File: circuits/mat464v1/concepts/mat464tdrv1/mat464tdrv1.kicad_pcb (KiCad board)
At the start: 2 copper layers, 107.2 x 67.3 mm, 41 parts, among them J1 Input 1, J10 GND VDC, J11 -VDC, J2 Input 2, J3 Input GND, J4 Zero crossing det, J5 Output 1, J6 Output 2, J7 Output GND, J8 Conn_WallSocket, J9 +VDC, Q1 BC547, Q2 BC547, U1 TL084

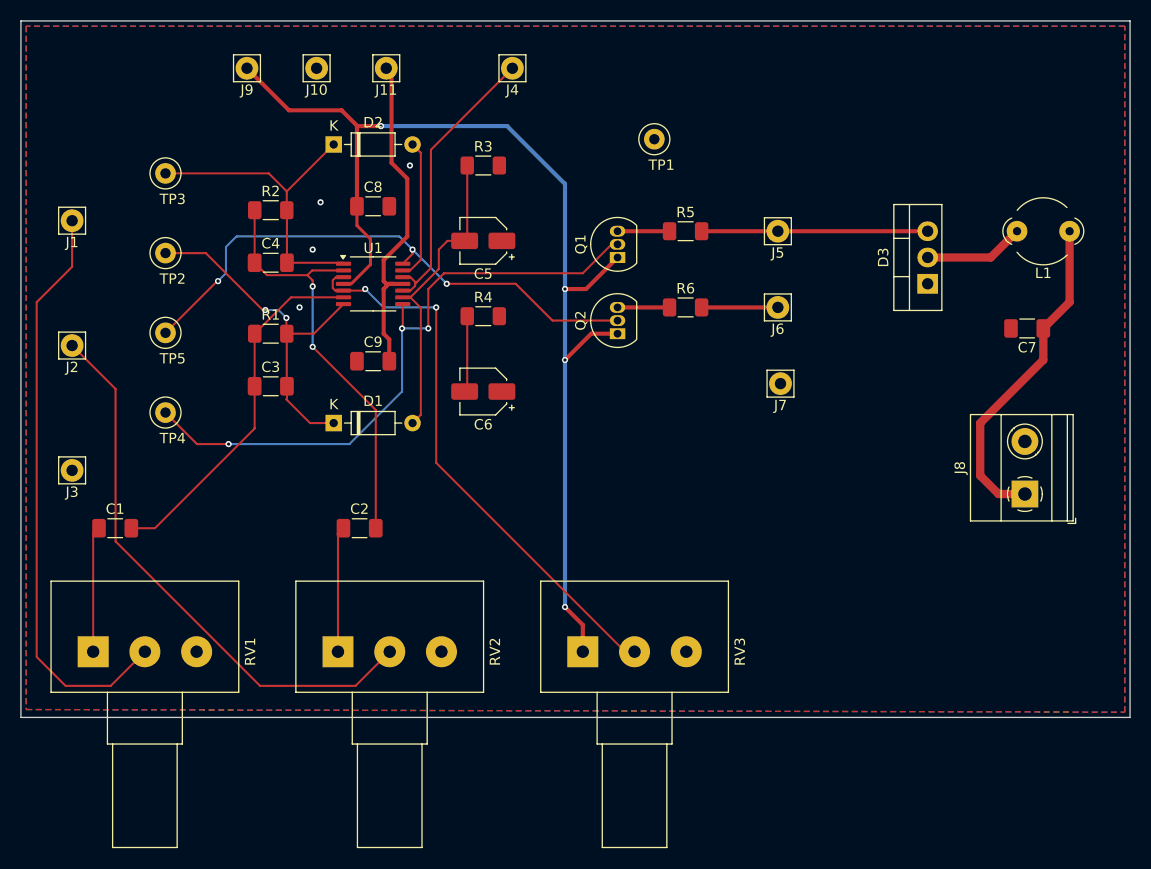
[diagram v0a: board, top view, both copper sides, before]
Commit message: Update the modern AT464 concept PCBs
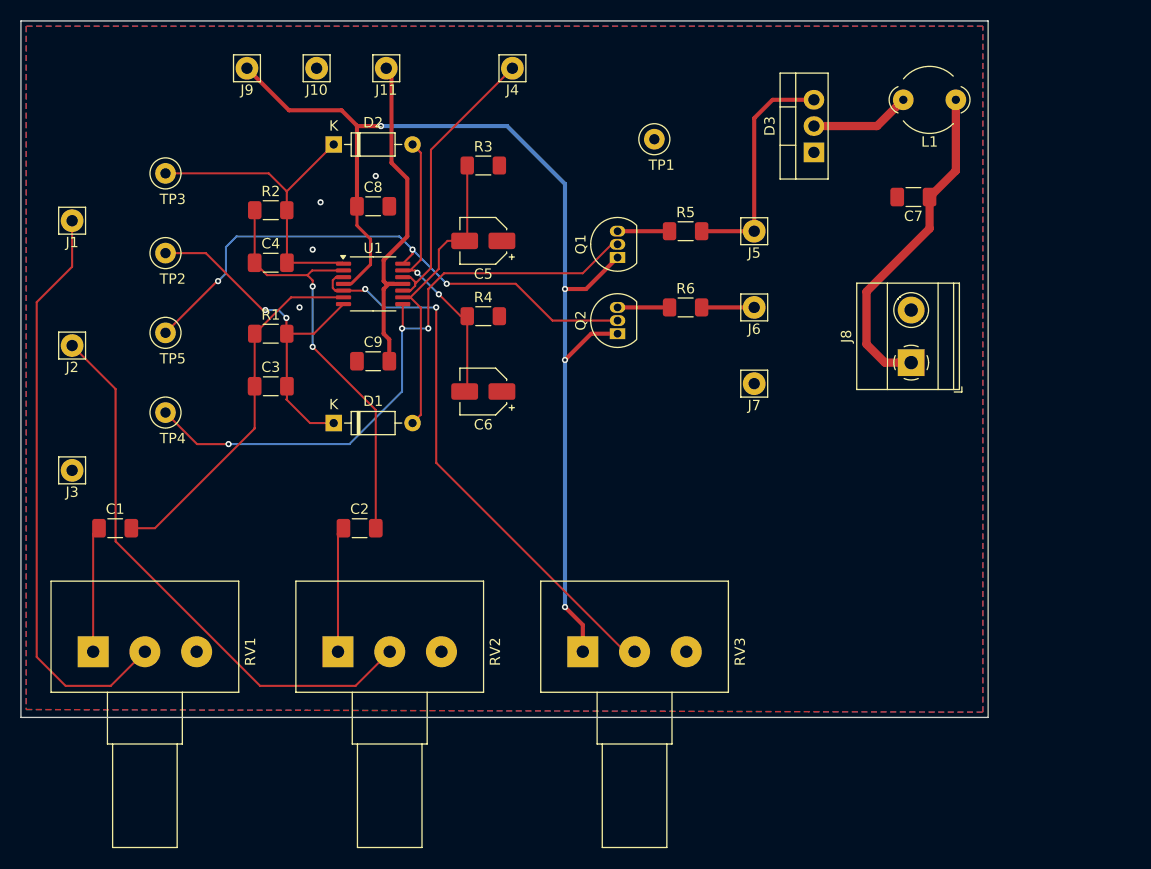
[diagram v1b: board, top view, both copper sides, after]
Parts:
- moved D3 16.8 mm to (134.3, 62.2)
- moved C7 16.8 mm to (143.9, 66.5)
- moved J8 16.8 mm to (143.7, 82.5)
- moved L1 16.8 mm to (148.0, 57.1)
- moved J7 2.54 mm to (128.5, 84.6)
- moved J5 2.29 mm to (128.5, 69.8)
- moved J6 2.29 mm to (128.5, 77.2)
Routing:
- net Net-(D2-A): track 21.0 -> 29.1 mm, vias 0 -> 2
- net Net-(J6-Pin_1): track 7.37 -> 5.08 mm
- net Net-(D3-G): track 21.8 -> 22.5 mm
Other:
- board size 107.2 x 67.3 mm -> 93.5 x 67.3 mm
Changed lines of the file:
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@@
 	(footprint "Capacitor_SMD:C_1206_3216Metric_Pad1.33x1.80mm_HandSolder"
 		(layer "F.Cu")
-		(at 154.9015 79.248 180)
+		(at 143.9085 66.548 180)
 		(descr "Capacitor SMD 1206 (3216 Metric), square (rectangular) end terminal, IPC_7351 nominal with elongated pad for handsoldering. (Body size source: IPC-SM-782 page 76, https://www.pcb-3d.com/wordpress/wp-content/uploads/ipc-sm-782a_amendment_1_and_2.pdf), generated with kicad-footprint-generator")
 		(tags "capacitor handsolder")
@@
 	(footprint "Connector_Pin:Pin_D1.1mm_L8.5mm_W2.5mm_FlatFork"
 		(layer "F.Cu")
-		(at 130.81 69.85)
+		(at 128.524 69.85)
 		(descr "solder Pin_ with flat fork, hole diameter 1.1mm, length 8.5mm, width 2.5mm")
 		(tags "solder Pin_ with flat fork")
@@
 	(footprint "Connector_Pin:Pin_D1.1mm_L8.5mm_W2.5mm_FlatFork"
 		(layer "F.Cu")
-		(at 130.81 77.216)
+		(at 128.524 77.216)
 		(descr "solder Pin_ with flat fork, hole diameter 1.1mm, length 8.5mm, width 2.5mm")
 		(tags "solder Pin_ with flat fork")
@@
 	(footprint "Package_TO_SOT_THT:TO-220-3_Vertical"
 		(layer "F.Cu")
-		(at 145.288 74.93 90)
+		(at 134.295 62.23 90)
 		(descr "TO-220-3, Vertical, RM 2.54mm, see https://www.vishay.com/docs/66542/to-220-1.pdf")
 		(tags "TO-220-3 Vertical RM 2.54mm")
@@
 	(footprint "TerminalBlock_Phoenix:TerminalBlock_Phoenix_MKDS-1,5-2-5.08_1x02_P5.08mm_Horizontal"
 		(layer "F.Cu")
-		(at 154.686 95.25 90)
+		(at 143.693 82.55 90)
 		(descr "Terminal Block Phoenix MKDS-1,5-2-5.08, 2 pins, pitch 5.08mm, size 10.2x9.8mm^2, drill diamater 1.3mm, pad diameter 2.6mm, see http://www.farnell.com/datasheets/100425.pdf, script-generated using https://github.com/pointhi/kicad-footprint-generator/scripts/TerminalBlock_Phoenix")
 		(tags "THT Terminal Block Phoenix MKDS-1,5-2-5.08 pitch 5.08mm size 10.2x9.8mm^2 drill 1.3mm pad 2.6mm")
@@
 	(footprint "Connector_Pin:Pin_D1.1mm_L8.5mm_W2.5mm_FlatFork"
 		(layer "F.Cu")
-		(at 131.064 84.582)
+		(at 128.524 84.582)
 		(descr "solder Pin_ with flat fork, hole diameter 1.1mm, length 8.5mm, width 2.5mm")
 		(tags "solder Pin_ with flat fork")
@@
 	(footprint "Ferrite_THT:LairdTech_28C0236-0JW-10"
 		(layer "F.Cu")
-		(at 159.004 69.85 180)
+		(at 148.011 57.15 180)
 		(descr "Ferrite, vertical, LairdTech 28C0236-0JW-10, https://assets.lairdtech.com/home/brandworld/files/28C0236-0JW-10.pdf, JW Miller core https://www.bourns.com/products/magnetic-products/j.w.-miller-through-hole-ferrite-beads-emi-filters")
 		(tags "Ferrite vertical LairdTech 28C0236-0JW-10")
@@
 	(gr_rect
 		(start 57.658 49.53)
-		(end 164.846 116.84)
+		(end 151.13 116.84)
 		(stroke
 			(width 0.05)
@@
 		(layer "User.1")
 		(pts
-			(xy 57.658 49.53) (xy 164.846 49.53)
+			(xy 151.13 116.84) (xy 151.13 49.53)
 		)
-		(height -6.858)
-		(gr_text "107.1880 mm"
-			(at 111.252 41.522 0)
+		(height 10.668)
+		(gr_text "67.3100 mm"
+			(at 160.648 83.185 90)
 			(layer "User.1")
 			(effects
@@
 		(layer "User.1")
 		(pts
-			(xy 164.846 116.84) (xy 164.846 49.53)
+			(xy 57.658 49.53) (xy 151.13 49.53)
 		)
-		(height 7.112)
-		(gr_text "67.3100 mm"
-			(at 170.808 83.185 90)
+		(height -7.62)
+		(gr_text "93.4720 mm"
+			(at 104.394 40.76 0)
 			(layer "User.1")
 			(effects
@@
 	)
 	(via
-		(at 95.25 63.5)
+		(at 86.614 67.056)
 		(size 0.6)
 		(drill 0.3)
@@
 	)
 	(via
-		(at 86.614 67.056)
+		(at 91.948 64.516)
 		(size 0.6)
 		(drill 0.3)
@@
 	)
 	(segment
+		(start 100.160666 78.062666)
+		(end 98.044 75.946)
+		(width 0.2)
+		(layer "F.Cu")
+		(net 9)
+	)
+	(segment
 		(start 95.2675 73.6425)
 		(end 94.5565 73.6425)
@@
 	)
 	(segment
+		(start 95.968735 73.870735)
+		(end 95.7405 73.6425)
+		(width 0.2)
+		(layer "F.Cu")
+		(net 9)
+	)
+	(segment
+		(start 95.7405 73.6425)
+		(end 94.5565 73.6425)
+		(width 0.2)
+		(layer "F.Cu")
+		(net 9)
+	)
+	(segment
 		(start 96.303999 62.267999)
 		(end 96.303999 72.606001)
@@
 	)
 	(segment
+		(start 100.79 78.062666)
+		(end 100.160666 78.062666)
+		(width 0.2)
+		(layer "F.Cu")
+		(net 9)
+	)
+	(segment
 		(start 100.79 85.094)
 		(end 100.54 85.344)
@@
 		(net 9)
 	)
+	(via
+		(at 98.044 75.946)
+		(size 0.6)
+		(drill 0.3)
+		(layers "F.Cu" "B.Cu")
+		(net 9)
+	)
+	(via
+		(at 95.968735 73.870735)
+		(size 0.6)
+		(drill 0.3)
+		(layers "F.Cu" "B.Cu")
+		(net 9)
+	)
 	(segment
-		(start 159.004 69.85)
-		(end 159.004 76.708)
+		(start 98.044 75.946)
+		(end 95.968735 73.870735)
+		(width 0.2)
+		(layer "B.Cu")
+		(net 9)
+	)
+	(segment
+		(start 148.011 57.15)
+		(end 148.011 64.008)
 		(width 0.8)
 		(layer "F.Cu")
@@
 	)
 	(segment
-		(start 150.368 88.392)
-		(end 150.368 93.472)
+		(start 139.375 75.692)
+		(end 139.375 80.772)
 		(width 0.8)
 		(layer "F.Cu")
@@
 	)
 	(segment
-		(start 156.464 79.248)
-		(end 156.464 82.296)
+		(start 145.471 66.548)
+		(end 145.471 69.596)
 		(width 0.8)
 		(layer "F.Cu")
@@
 	)
 	(segment
-		(start 150.368 93.472)
-		(end 152.146 95.25)
+		(start 139.375 80.772)
+		(end 141.153 82.55)
 		(width 0.8)
 		(layer "F.Cu")
@@
 	)
 	(segment
-		(start 159.004 76.708)
-		(end 156.464 79.248)
+		(start 148.011 64.008)
+		(end 145.471 66.548)
 		(width 0.8)
 		(layer "F.Cu")
@@
 	)
 	(segment
-		(start 152.146 95.25)
-		(end 154.686 95.25)
+		(start 141.153 82.55)
+		(end 143.693 82.55)
 		(width 0.8)
 		(layer "F.Cu")
@@
 	)
 	(segment
-		(start 156.464 82.296)
-		(end 150.368 88.392)
+		(start 145.471 69.596)
+		(end 139.375 75.692)
 		(width 0.8)
 		(layer "F.Cu")
@@
 	)
 	(segment
-		(start 145.288 72.39)
-		(end 151.384 72.39)
+		(start 134.295 59.69)
+		(end 140.391 59.69)
 		(width 0.8)
 		(layer "F.Cu")
@@
 	)
 	(segment
-		(start 151.384 72.39)
-		(end 153.924 69.85)
+		(start 140.391 59.69)
+		(end 142.931 57.15)
 		(width 0.8)
 		(layer "F.Cu")
@@
 	)
 	(segment
-		(start 123.444 69.85)
-		(end 130.81 69.85)
+		(start 128.524 58.928)
+		(end 130.302 57.15)
+		(width 0.4)
+		(layer "F.Cu")
+		(net 14)
+	)
+	(segment
+		(start 130.302 57.15)
+		(end 134.295 57.15)
 		(width 0.4)
 		(layer "F.Cu")
@@
 	)
 	(segment
-		(start 130.81 69.85)
-		(end 145.288 69.85)
+		(start 128.524 69.85)
+		(end 128.524 58.928)
+		(width 0.4)
+		(layer "F.Cu")
+		(net 14)
+	)
+	(segment
+		(start 123.444 69.85)
+		(end 128.524 69.85)
 		(width 0.4)
 		(layer "F.Cu")
@@
 	(segment
 		(start 123.444 77.216)
-		(end 130.81 77.216)
+		(end 128.524 77.216)
 		(width 0.4)
 		(layer "F.Cu")
@@
 		(polygon
 			(pts
-				(xy 58.166 50.038) (xy 58.166 116.078) (xy 164.338 116.332) (xy 164.338 50.038)
+				(xy 58.166 50.038) (xy 58.166 116.078) (xy 150.622 116.332) (xy 150.622 50.038)
 			)
 		)
@@
 		(polygon
 			(pts
-				(xy 58.166 50.038) (xy 58.166 116.078) (xy 164.338 116.332) (xy 164.338 50.038)
+				(xy 58.166 50.038) (xy 58.166 116.078) (xy 150.622 116.332) (xy 150.622 50.038)
 			)
 		)
